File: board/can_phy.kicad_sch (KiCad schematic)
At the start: 5 parts, among them U1 MCP2542FDT

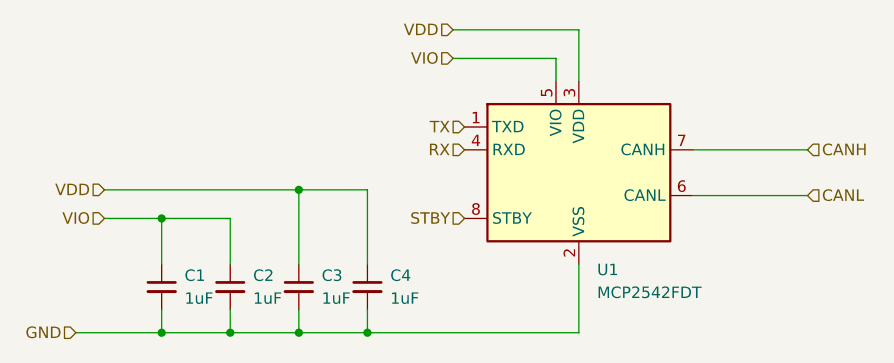
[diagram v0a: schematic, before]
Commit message: renamed subsheet to work better in compositions
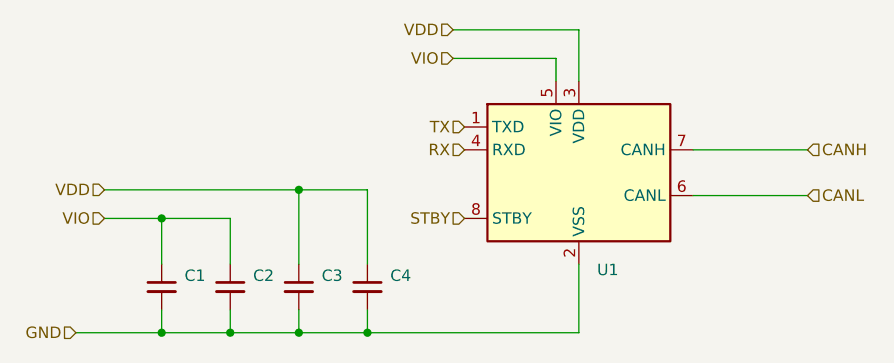
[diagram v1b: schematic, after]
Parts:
- C1, C2, C3, C4: value 1uF -> (none); footprint Capacitor_SMD:C_0603_1608Metric -> (none)
- U1: value MCP2542FDT -> (none); footprint Package_SO:SOIC-8_3.9x4.9mm_P1.27mm -> (none)
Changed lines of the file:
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@@
       (effects (font (size 1.27 1.27)) (justify left))
     )
-    (property "Value" "MCP2542FDT" (id 1) (at 139.8144 99.06 0)
+    (property "Value" "" (id 1) (at 139.8144 99.06 0)
       (effects (font (size 1.27 1.27)) (justify left))
     )
-    (property "Footprint" "Package_SO:SOIC-8_3.9x4.9mm_P1.27mm" (id 2) (at 137.795 98.425 0)
+    (property "Footprint" "" (id 2) (at 137.795 98.425 0)
       (effects (font (size 1.27 1.27) italic) hide)
     )
@@
       (effects (font (size 1.27 1.27)) (justify left))
     )
-    (property "Value" "1uF" (id 1) (at 101.6 99.7012 0)
+    (property "Value" "" (id 1) (at 101.6 99.7012 0)
       (effects (font (size 1.27 1.27)) (justify left))
     )
-    (property "Footprint" "Capacitor_SMD:C_0603_1608Metric" (id 2) (at 99.06 98.425 0)
+    (property "Footprint" "" (id 2) (at 99.06 98.425 0)
       (effects (font (size 1.27 1.27)) hide)
     )
@@
       (effects (font (size 1.27 1.27)) (justify left))
     )
-    (property "Value" "1uF" (id 1) (at 109.22 99.7012 0)
+    (property "Value" "" (id 1) (at 109.22 99.7012 0)
       (effects (font (size 1.27 1.27)) (justify left))
     )
-    (property "Footprint" "Capacitor_SMD:C_0603_1608Metric" (id 2) (at 106.68 98.425 0)
+    (property "Footprint" "" (id 2) (at 106.68 98.425 0)
       (effects (font (size 1.27 1.27)) hide)
     )
@@
       (effects (font (size 1.27 1.27)) (justify left))
     )
-    (property "Value" "1uF" (id 1) (at 93.98 99.7012 0)
+    (property "Value" "" (id 1) (at 93.98 99.7012 0)
       (effects (font (size 1.27 1.27)) (justify left))
     )
-    (property "Footprint" "Capacitor_SMD:C_0603_1608Metric" (id 2) (at 91.44 98.425 0)
+    (property "Footprint" "" (id 2) (at 91.44 98.425 0)
       (effects (font (size 1.27 1.27)) hide)
     )
@@
       (effects (font (size 1.27 1.27)) (justify left))
     )
-    (property "Value" "1uF" (id 1) (at 116.84 99.7012 0)
+    (property "Value" "" (id 1) (at 116.84 99.7012 0)
       (effects (font (size 1.27 1.27)) (justify left))
     )
-    (property "Footprint" "Capacitor_SMD:C_0603_1608Metric" (id 2) (at 114.3 98.425 0)
+    (property "Footprint" "" (id 2) (at 114.3 98.425 0)
       (effects (font (size 1.27 1.27)) hide)
     )
